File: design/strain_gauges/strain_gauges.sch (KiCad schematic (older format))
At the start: 28 parts, among them J1 Conn_01x03, J2 Conn_01x03, J3 Conn_01x08, P1 CONN_01X02, P2 CONN_01X04, P3 CONN_01X04, P4 CONN_01X04, P5 CONN_01X04, Q1 Q_PNP_BCE, U1 LT1460-10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

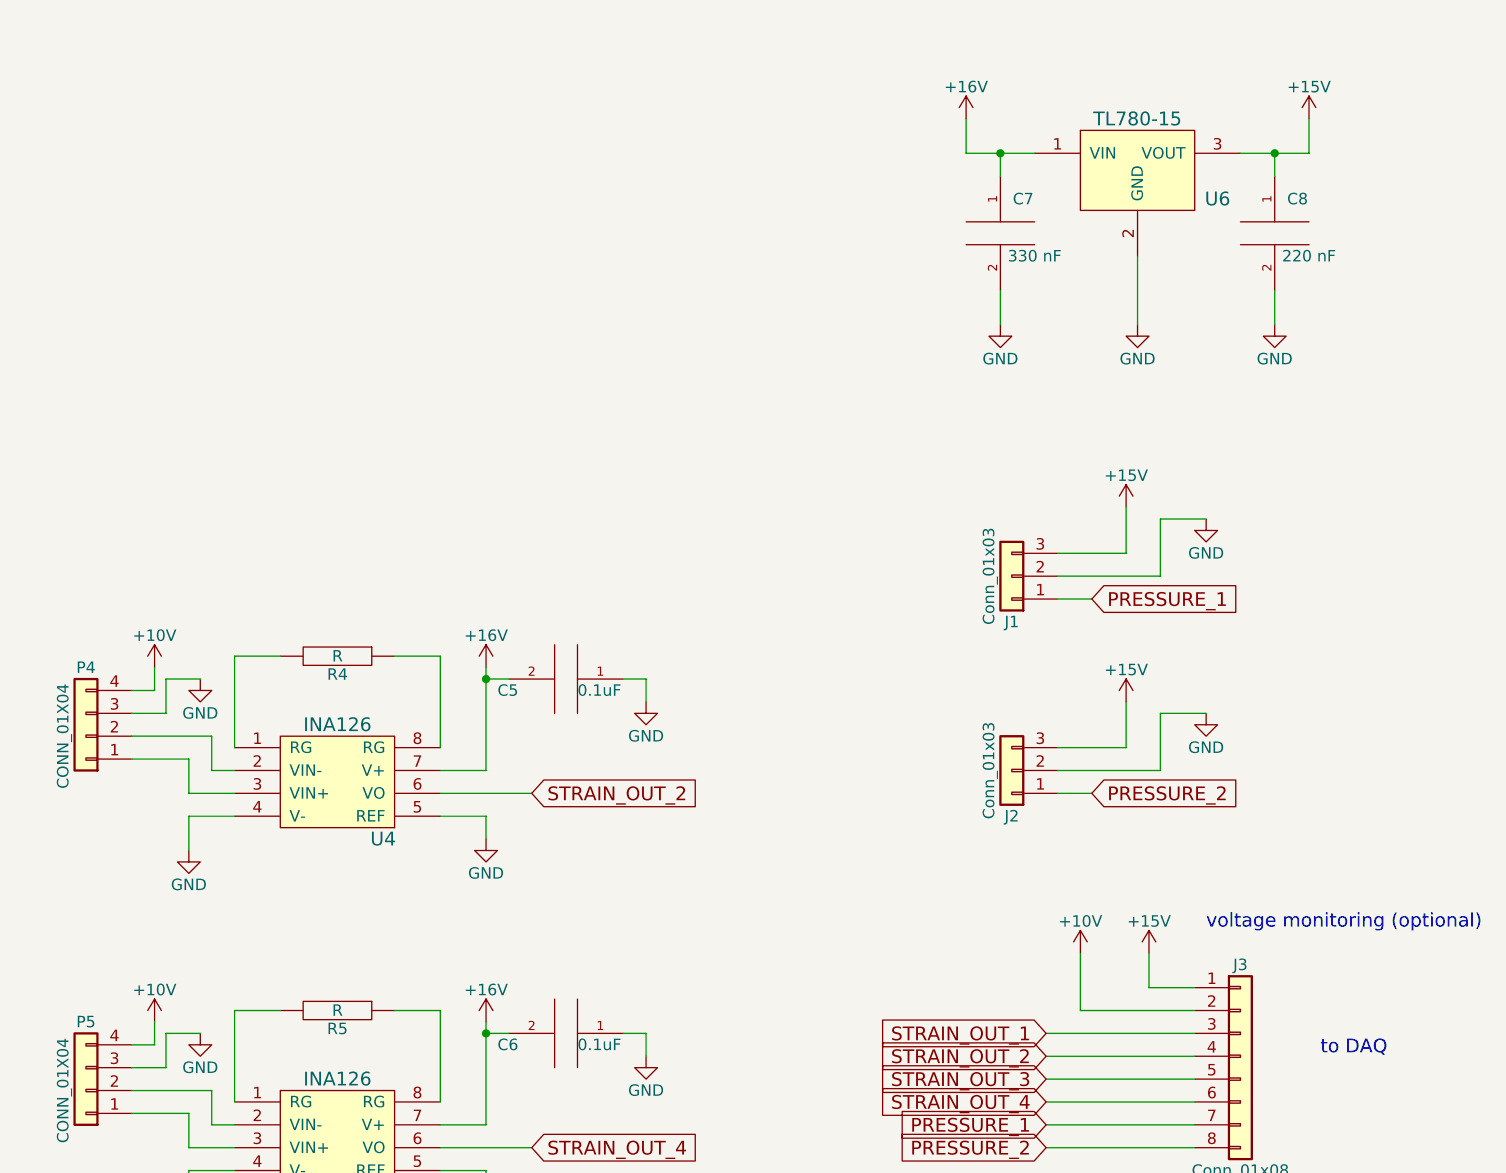
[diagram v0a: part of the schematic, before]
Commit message: Fix voltage monitoring, add gitignore
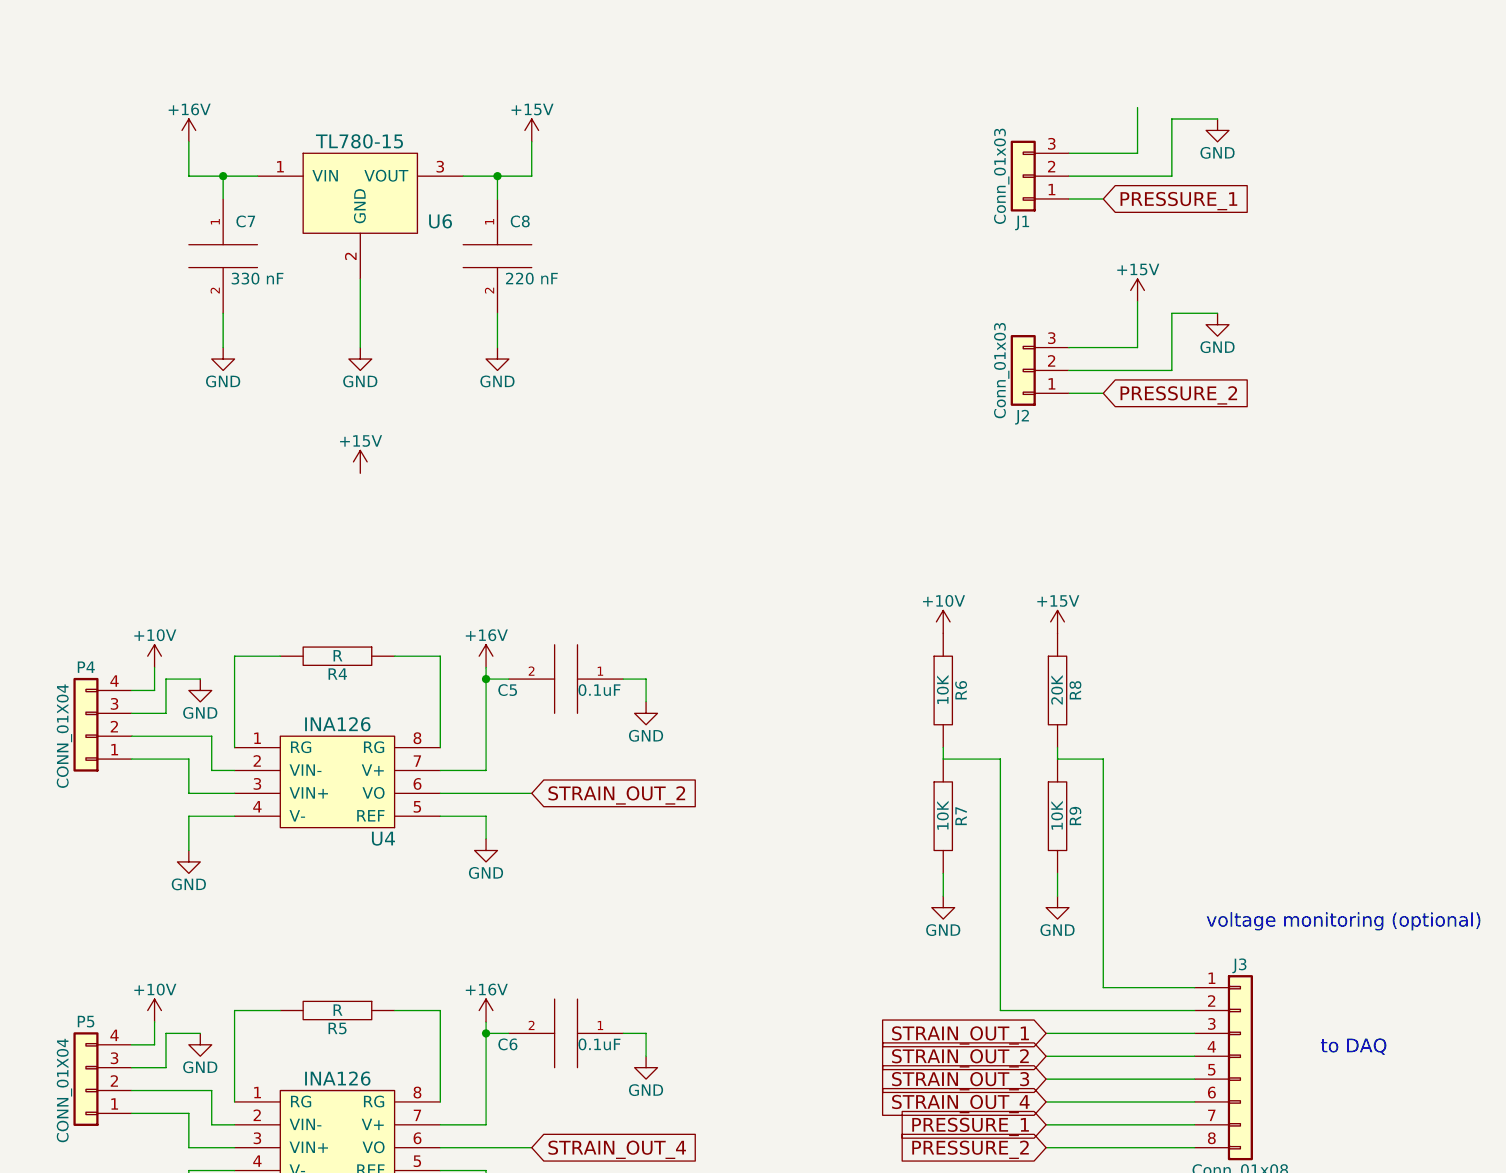
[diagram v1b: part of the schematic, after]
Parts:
- added R6, R7, R9: 10K, symbol R
- added R8: 20K, symbol R
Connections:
- wire segments 146 -> 152
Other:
- moved on the sheet: C7, C8, J1, J2, U6

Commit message: Fix strain gauge schematic
- swap out pnp transistor for a higher power one
- misc rearrangments
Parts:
- removed Q1: Q_PNP_BCE, TO_SOT_Packages_THT:TO-92_Inline_Narrow_Oval, symbol Q_PNP_BCE
- added Q1: BC640, TO_SOT_Packages_THT:TO-92_Inline_Narrow_Oval, symbol Q_PNP_ECB
- R6, R7, R8, R9: footprint (none) -> Resistors_SMD:R_0805_HandSoldering
- U6: footprint TO_SOT_Packages_THT:TO-220-3_Horizontal -> TO_SOT_Packages_THT:TO-220-3_Vertical
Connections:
- wire segments 152 -> 153

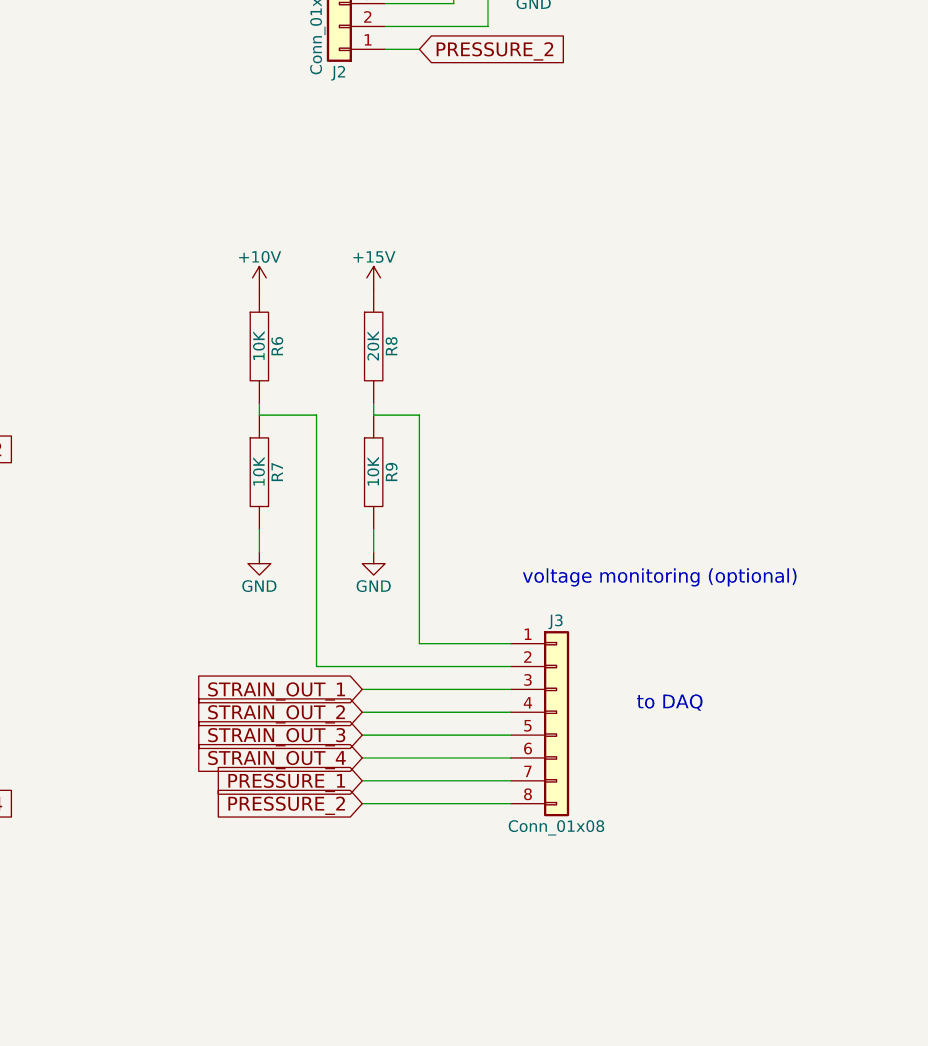
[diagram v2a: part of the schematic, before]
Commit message: Preliminary board layout (no tracks)
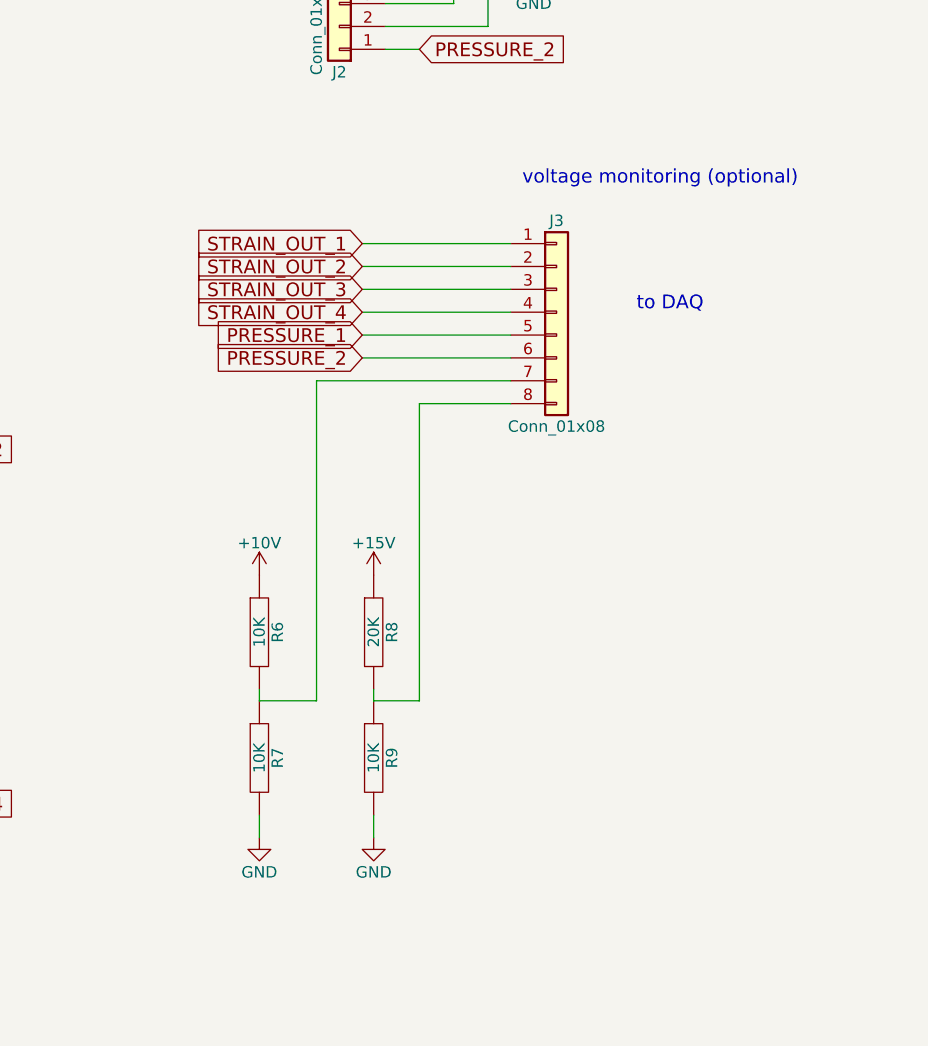
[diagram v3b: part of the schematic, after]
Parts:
- J1, J2: footprint Socket_Strips:Socket_Strip_Straight_1x03_Pitch2.54mm -> Connectors_Phoenix:PhoenixContact_MCV-G_03x3.50mm_Vertical
- J3: footprint Socket_Strips:Socket_Strip_Straight_1x08_Pitch2.54mm -> Connectors_Phoenix:PhoenixContact_MCV-G_08x3.50mm_Vertical
- P1: footprint Socket_Strips:Socket_Strip_Straight_1x02_Pitch2.54mm -> Connectors_Phoenix:PhoenixContact_MCV-G_02x3.50mm_Vertical
- P2, P3, P4, P5: footprint Socket_Strips:Socket_Strip_Straight_1x04_Pitch2.54mm -> Connectors_Phoenix:PhoenixContact_MCV-G_04x3.50mm_Vertical
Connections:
- net PRESSURE_1: now also J3.5 (Pin_5); no longer J3.7 (Pin_7)
- net PRESSURE_2: now also J3.6 (Pin_6); no longer J3.8 (Pin_8)
- net STRAIN_OUT_1: now also J3.1 (Pin_1); no longer J3.3 (Pin_3)
- net STRAIN_OUT_2: now also J3.2 (Pin_2); no longer J3.4 (Pin_4)
- net STRAIN_OUT_3: now also J3.3 (Pin_3); no longer J3.5 (Pin_5)
- net STRAIN_OUT_4: now also J3.4 (Pin_4); no longer J3.6 (Pin_6)
- net at R8.2, R9.1: now also J3.8 (Pin_8); no longer J3.1 (Pin_1)
- net at R6.2, R7.1: now also J3.7 (Pin_7); no longer J3.2 (Pin_2)
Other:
- moved on the sheet: J3, R6, R7, R8, R9
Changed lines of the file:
@@
 F 0 "P1" H 1200 1200 50  0000 C CNN
 F 1 "CONN_01X02" V 1300 1050 50  0000 C CNN
-F 2 "Socket_Strips:Socket_Strip_Straight_1x02_Pitch2.54mm" H 1200 1050 50  0001 C CNN
+F 2 "Connectors_Phoenix:PhoenixContact_MCV-G_02x3.50mm_Vertical" H 1200 1050 50  0001 C CNN
 F 3 "" H 1200 1050 50  0000 C CNN
 	1    1200 1050
@@
 F 0 "P2" H 1200 3500 50  0000 C CNN
 F 1 "CONN_01X04" V 1300 3800 50  0000 C CNN
-F 2 "Socket_Strips:Socket_Strip_Straight_1x04_Pitch2.54mm" H 1200 3800 50  0001 C CNN
+F 2 "Connectors_Phoenix:PhoenixContact_MCV-G_04x3.50mm_Vertical" H 1200 3800 50  0001 C CNN
 F 3 "" H 1200 3800 50  0000 C CNN
 	1    1200 3800
@@
 F 0 "P3" H 1200 5050 50  0000 C CNN
 F 1 "CONN_01X04" V 1300 5350 50  0000 C CNN
-F 2 "Socket_Strips:Socket_Strip_Straight_1x04_Pitch2.54mm" H 1200 5350 50  0001 C CNN
+F 2 "Connectors_Phoenix:PhoenixContact_MCV-G_04x3.50mm_Vertical" H 1200 5350 50  0001 C CNN
 F 3 "" H 1200 5350 50  0000 C CNN
 	1    1200 5350
@@
 F 0 "P4" H 4550 3500 50  0000 C CNN
 F 1 "CONN_01X04" V 4650 3800 50  0000 C CNN
-F 2 "Socket_Strips:Socket_Strip_Straight_1x04_Pitch2.54mm" H 4550 3800 50  0001 C CNN
+F 2 "Connectors_Phoenix:PhoenixContact_MCV-G_04x3.50mm_Vertical" H 4550 3800 50  0001 C CNN
 F 3 "" H 4550 3800 50  0000 C CNN
 	1    4550 3800
@@
 F 0 "P5" H 4550 5050 50  0000 C CNN
 F 1 "CONN_01X04" V 4650 5350 50  0000 C CNN
-F 2 "Socket_Strips:Socket_Strip_Straight_1x04_Pitch2.54mm" H 4550 5350 50  0001 C CNN
+F 2 "Connectors_Phoenix:PhoenixContact_MCV-G_04x3.50mm_Vertical" H 4550 5350 50  0001 C CNN
 F 3 "" H 4550 5350 50  0000 C CNN
 	1    4550 5350
@@
 F 0 "J1" H 8650 1550 50  0000 C CNN
 F 1 "Conn_01x03" V 8750 1350 50  0000 C CNN
-F 2 "Socket_Strips:Socket_Strip_Straight_1x03_Pitch2.54mm" H 8650 1350 50  0001 C CNN
+F 2 "Connectors_Phoenix:PhoenixContact_MCV-G_03x3.50mm_Vertical" H 8650 1350 50  0001 C CNN
 F 3 "" H 8650 1350 50  0001 C CNN
 	1    8650 1350
@@
 F 0 "J2" H 8650 2400 50  0000 C CNN
 F 1 "Conn_01x03" V 8750 2200 50  0000 C CNN
-F 2 "Socket_Strips:Socket_Strip_Straight_1x03_Pitch2.54mm" H 8650 2200 50  0001 C CNN
+F 2 "Connectors_Phoenix:PhoenixContact_MCV-G_03x3.50mm_Vertical" H 8650 2200 50  0001 C CNN
 F 3 "" H 8650 2200 50  0001 C CNN
 	1    8650 2200
@@
 L Conn_01x08 J3
 U 1 1 5A2F4056
-P 9600 5200
-F 0 "J3" H 9600 5600 50  0000 C CNN
-F 1 "Conn_01x08" H 9600 4700 50  0000 C CNN
-F 2 "Socket_Strips:Socket_Strip_Straight_1x08_Pitch2.54mm" H 9600 5200 50  0001 C CNN
-F 3 "" H 9600 5200 50  0001 C CNN
-	1    9600 5200
-	1    0    0    -1
-$EndComp
-Text GLabel 8750 5100 0    60   Input ~ 0
+P 9600 3450
+F 0 "J3" H 9600 3850 50  0000 C CNN
+F 1 "Conn_01x08" H 9600 2950 50  0000 C CNN
+F 2 "Connectors_Phoenix:PhoenixContact_MCV-G_08x3.50mm_Vertical" H 9600 3450 50  0001 C CNN
+F 3 "" H 9600 3450 50  0001 C CNN
+	1    9600 3450
+	1    0    0    -1
+$EndComp
+Text GLabel 8750 3150 0    60   Input ~ 0
 STRAIN_OUT_1
-Text GLabel 8750 5200 0    60   Input ~ 0
+Text GLabel 8750 3250 0    60   Input ~ 0
 STRAIN_OUT_2
-Text GLabel 8750 5300 0    60   Input ~ 0
+Text GLabel 8750 3350 0    60   Input ~ 0
 STRAIN_OUT_3
-Text GLabel 8750 5400 0    60   Input ~ 0
+Text GLabel 8750 3450 0    60   Input ~ 0
 STRAIN_OUT_4
-Text GLabel 8750 5500 0    60   Input ~ 0
+Text GLabel 8750 3550 0    60   Input ~ 0
 PRESSURE_1
-Text GLabel 8750 5600 0    60   Input ~ 0
+Text GLabel 8750 3650 0    60   Input ~ 0
 PRESSURE_2
-Text Notes 9950 5200 0    60   ~ 0
+Text Notes 9950 3450 0    60   ~ 0
 to DAQ
-Text Notes 9450 4650 0    60   ~ 0
+Text Notes 9450 2900 0    60   ~ 0
 voltage monitoring (optional)
 $Comp
@@
 $EndComp
 Wire Wire Line
-	8750 5100 9400 5100
-Wire Wire Line
-	8750 5200 9400 5200
-Wire Wire Line
-	8750 5300 9400 5300
-Wire Wire Line
-	8750 5400 9400 5400
-Wire Wire Line
-	8750 5500 9400 5500
-Wire Wire Line
-	8750 5600 9400 5600
+	8750 3150 9400 3150
+Wire Wire Line
+	8750 3250 9400 3250
+Wire Wire Line
+	8750 3350 9400 3350
+Wire Wire Line
+	8750 3450 9400 3450
+Wire Wire Line
+	8750 3550 9400 3550
+Wire Wire Line
+	8750 3650 9400 3650
 Wire Wire Line
 	3650 3650 3650 3550
@@
 L +10V #PWR038
 U 1 1 5A4C1972
-P 8300 3350
-F 0 "#PWR038" H 8300 3200 50  0001 C CNN
-F 1 "+10V" H 8300 3490 50  0000 C CNN
-F 2 "" H 8300 3350 50  0000 C CNN
-F 3 "" H 8300 3350 50  0000 C CNN
-	1    8300 3350
+P 8300 4600
+F 0 "#PWR038" H 8300 4450 50  0001 C CNN
+F 1 "+10V" H 8300 4740 50  0000 C CNN
+F 2 "" H 8300 4600 50  0000 C CNN
+F 3 "" H 8300 4600 50  0000 C CNN
+	1    8300 4600
 	1    0    0    -1
 $EndComp
@@
 L R R6
 U 1 1 5A4C19DA
-P 8300 3600
-F 0 "R6" V 8380 3600 50  0000 C CNN
-F 1 "10K" V 8300 3600 50  0000 C CNN
-F 2 "Resistors_SMD:R_0805_HandSoldering" H 8300 3600 50  0001 C CNN
-F 3 "" H 8300 3600 50  0001 C CNN
-	1    8300 3600
+P 8300 4850
+F 0 "R6" V 8380 4850 50  0000 C CNN
+F 1 "10K" V 8300 4850 50  0000 C CNN
+F 2 "Resistors_SMD:R_0805_HandSoldering" H 8300 4850 50  0001 C CNN
+F 3 "" H 8300 4850 50  0001 C CNN
+	1    8300 4850
 	1    0    0    -1
 $EndComp
@@
 L R R7
 U 1 1 5A4C1A4B
-P 8300 4150
-F 0 "R7" V 8380 4150 50  0000 C CNN
-F 1 "10K" V 8300 4150 50  0000 C CNN
-F 2 "Resistors_SMD:R_0805_HandSoldering" H 8300 4150 50  0001 C CNN
-F 3 "" H 8300 4150 50  0001 C CNN
-	1    8300 4150
-	1    0    0    -1
-$EndComp
-Wire Wire Line
-	8300 3850 8300 3900
+P 8300 5400
+F 0 "R7" V 8380 5400 50  0000 C CNN
+F 1 "10K" V 8300 5400 50  0000 C CNN
+F 2 "Resistors_SMD:R_0805_HandSoldering" H 8300 5400 50  0001 C CNN
+F 3 "" H 8300 5400 50  0001 C CNN
+	1    8300 5400
+	1    0    0    -1
+$EndComp
+Wire Wire Line
+	8300 5100 8300 5150
 $Comp
 L GND #PWR039
 U 1 1 5A4C274E
-P 8300 4500
-F 0 "#PWR039" H 8300 4250 50  0001 C CNN
-F 1 "GND" H 8300 4350 50  0000 C CNN
-F 2 "" H 8300 4500 50  0001 C CNN
-F 3 "" H 8300 4500 50  0001 C CNN
-	1    8300 4500
-	1    0    0    -1
-$EndComp
-Wire Wire Line
-	8300 4500 8300 4400
+P 8300 5750
+F 0 "#PWR039" H 8300 5500 50  0001 C CNN
+F 1 "GND" H 8300 5600 50  0000 C CNN
+F 2 "" H 8300 5750 50  0001 C CNN
+F 3 "" H 8300 5750 50  0001 C CNN
+	1    8300 5750
+	1    0    0    -1
+$EndComp
+Wire Wire Line
+	8300 5750 8300 5650
 $Comp
 L R R8
 U 1 1 5A4C2B16
-P 8800 3600
-F 0 "R8" V 8880 3600 50  0000 C CNN
-F 1 "20K" V 8800 3600 50  0000 C CNN
-F 2 "Resistors_SMD:R_0805_HandSoldering" H 8800 3600 50  0001 C CNN
-F 3 "" H 8800 3600 50  0001 C CNN
-	1    8800 3600
+P 8800 4850
+F 0 "R8" V 8880 4850 50  0000 C CNN
+F 1 "20K" V 8800 4850 50  0000 C CNN
+F 2 "Resistors_SMD:R_0805_HandSoldering" H 8800 4850 50  0001 C CNN
+F 3 "" H 8800 4850 50  0001 C CNN
+	1    8800 4850
 	1    0    0    -1
 $EndComp
@@
 L R R9
 U 1 1 5A4C2B1C
-P 8800 4150
-F 0 "R9" V 8880 4150 50  0000 C CNN
-F 1 "10K" V 8800 4150 50  0000 C CNN
-F 2 "Resistors_SMD:R_0805_HandSoldering" H 8800 4150 50  0001 C CNN
-F 3 "" H 8800 4150 50  0001 C CNN
-	1    8800 4150
-	1    0    0    -1
-$EndComp
-Wire Wire Line
-	8800 3850 8800 3900
+P 8800 5400
+F 0 "R9" V 8880 5400 50  0000 C CNN
+F 1 "10K" V 8800 5400 50  0000 C CNN
+F 2 "Resistors_SMD:R_0805_HandSoldering" H 8800 5400 50  0001 C CNN
+F 3 "" H 8800 5400 50  0001 C CNN
+	1    8800 5400
+	1    0    0    -1
+$EndComp
+Wire Wire Line
+	8800 5100 8800 5150
 $Comp
 L GND #PWR040
 U 1 1 5A4C2B23
-P 8800 4500
-F 0 "#PWR040" H 8800 4250 50  0001 C CNN
-F 1 "GND" H 8800 4350 50  0000 C CNN
-F 2 "" H 8800 4500 50  0001 C CNN
-F 3 "" H 8800 4500 50  0001 C CNN
-	1    8800 4500
-	1    0    0    -1
-$EndComp
-Wire Wire Line
-	8800 4500 8800 4400
+P 8800 5750
+F 0 "#PWR040" H 8800 5500 50  0001 C CNN
+F 1 "GND" H 8800 5600 50  0000 C CNN
+F 2 "" H 8800 5750 50  0001 C CNN
+F 3 "" H 8800 5750 50  0001 C CNN
+	1    8800 5750
+	1    0    0    -1
+$EndComp
+Wire Wire Line
+	8800 5750 8800 5650
 $Comp
 L +15V #PWR041
 U 1 1 5A4C2B8F
-P 8800 3350
-F 0 "#PWR041" H 8800 3200 50  0001 C CNN
-F 1 "+15V" H 8800 3490 50  0000 C CNN
-F 2 "" H 8800 3350 50  0000 C CNN
-F 3 "" H 8800 3350 50  0000 C CNN
-	1    8800 3350
-	1    0    0    -1
-$EndComp
-Wire Wire Line
-	8300 3900 8550 3900
-Wire Wire Line
-	8550 3900 8550 5000
-Wire Wire Line
-	8550 5000 9400 5000
-Wire Wire Line
-	8800 3900 9000 3900
-Wire Wire Line
-	9000 3900 9000 4900
-Wire Wire Line
-	9000 4900 9400 4900
+P 8800 4600
+F 0 "#PWR041" H 8800 4450 50  0001 C CNN
+F 1 "+15V" H 8800 4740 50  0000 C CNN
+F 2 "" H 8800 4600 50  0000 C CNN
+F 3 "" H 8800 4600 50  0000 C CNN
+	1    8800 4600
+	1    0    0    -1
+$EndComp
+Wire Wire Line
+	8300 5150 8550 5150
+Wire Wire Line
+	8800 5150 9000 5150
 Wire Wire Line
 	3150 950  3150 1350
@@
 	1    0    0    -1
 $EndComp
+Wire Wire Line
+	8550 5150 8550 3750
+Wire Wire Line
+	8550 3750 9400 3750
+Wire Wire Line
+	9000 5150 9000 3850
+Wire Wire Line
+	9000 3850 9400 3850
 $EndSCHEMATC
